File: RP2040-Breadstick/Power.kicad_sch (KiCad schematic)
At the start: 11 parts, among them IC501 LM66200DRLR, U501 MIC5528-3.3YMT-TR

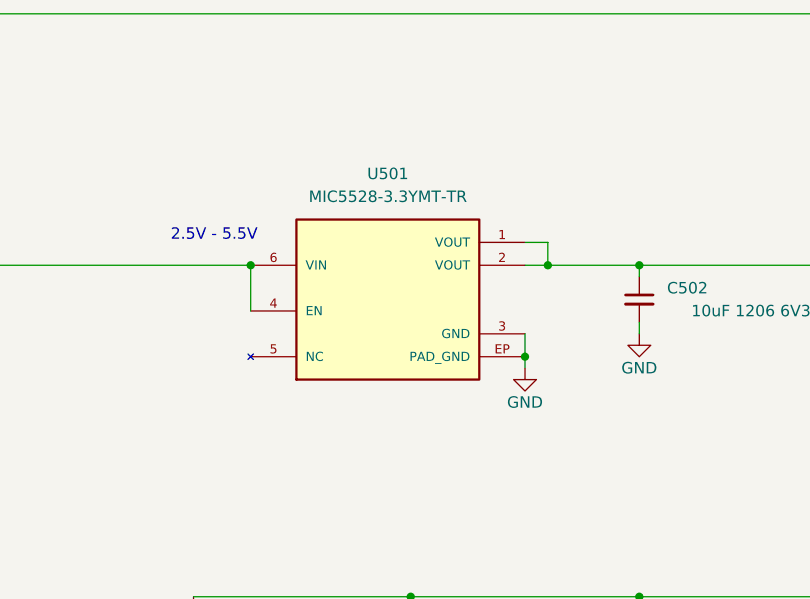
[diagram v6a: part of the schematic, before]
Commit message: Finished assigning I/O pins, perfect is the enemy of good.
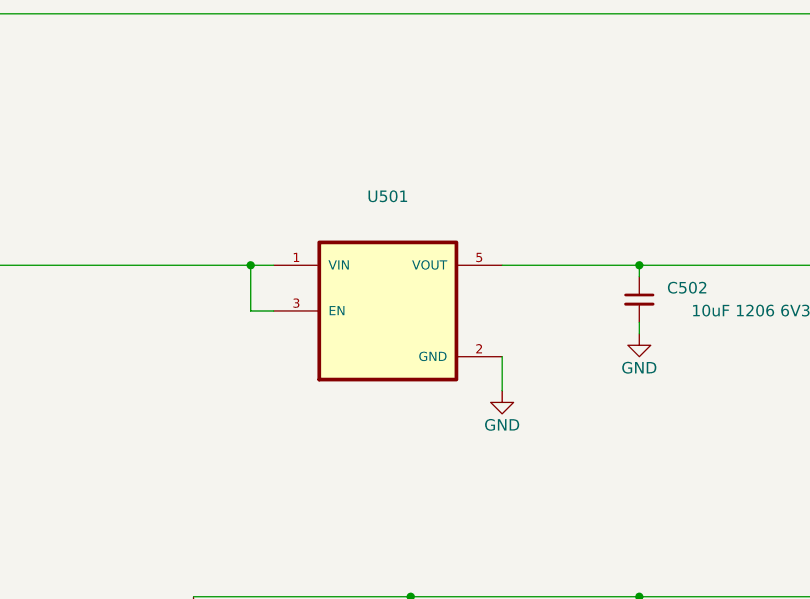
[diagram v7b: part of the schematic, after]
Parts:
- removed U501: MIC5528-3.3YMT-TR, SON40P120X120X60-7N, symbol MIC5528-3.3YMT-TR:MIC5528-3.3YMT-TR
- added U501: (no value), symbol AP2112K-3.3TRG1:AP2112K-3.3TRG1
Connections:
- net 3V3_LDO: now also U501.5 (VOUT)
- net GND: now also U501.2 (GND)
- net VHI: now also U501.1 (VIN), U501.3 (EN)
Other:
- note removed: "2.5V - 5.5V"

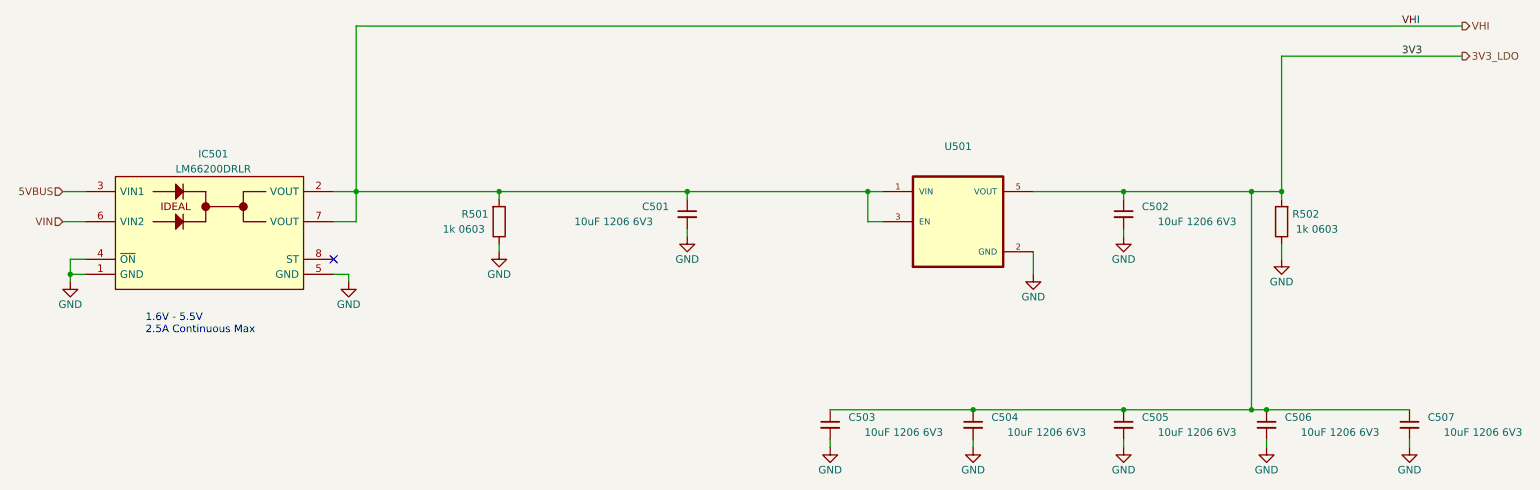
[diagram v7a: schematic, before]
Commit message: replaced switches, upsized some passives to 0603
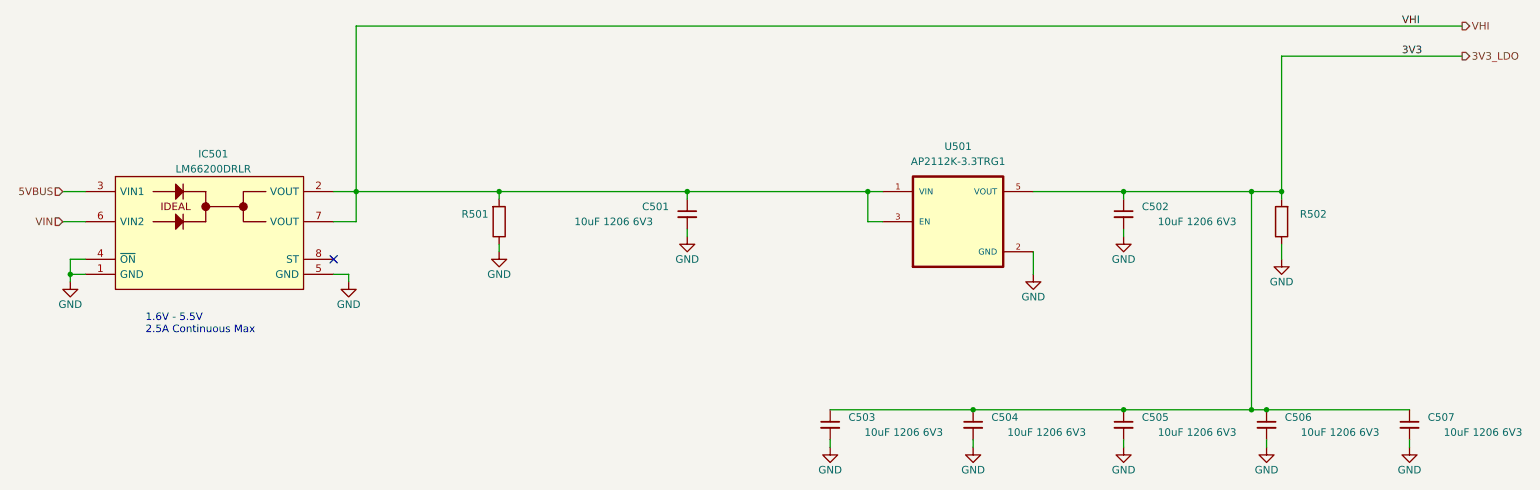
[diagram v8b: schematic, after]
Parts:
- R501: value 1k 0603 -> (none); footprint Resistor_SMD:R_0603_1608Metric -> (none)
- R502: value 1k 0603 -> (none)
- U501: value (none) -> AP2112K-3.3TRG1; footprint (none) -> AP2112K-3:SOT95P285X140-5N
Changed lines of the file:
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@@
   (symbol (lib_id "Device:R") (at 233.68 81.28 180) (unit 1)
     (in_bom yes) (on_board yes)
-    (property "Reference" "R502" (id 0) (at 240.03 80.01 0)
-      (effects (font (size 1.27 1.27)) (justify left))
-    )
-    (property "Value" "1k 0603" (id 1) (at 243.205 82.55 0)
+    (property "Reference" "R502" (id 0) (at 241.3 80.01 0)
+      (effects (font (size 1.27 1.27)) (justify left))
+    )
+    (property "Value" "" (id 1) (at 245.11 82.55 0)
       (effects (font (size 1.27 1.27)) (justify left))
     )
@@
     (in_bom yes) (on_board yes) (fields_autoplaced)
     (property "Reference" "U501" (id 0) (at 179.07 68.58 0))
-    (property "Value" "" (id 1) (at 179.07 71.12 0))
-    (property "Footprint" "" (id 2) (at 179.07 81.28 0)
+    (property "Value" "AP2112K-3.3TRG1" (id 1) (at 179.07 71.12 0))
+    (property "Footprint" "AP2112K-3:SOT95P285X140-5N" (id 2) (at 179.07 81.28 0)
       (effects (font (size 1.27 1.27)) (justify bottom) hide)
     )
@@
       (effects (font (size 1.27 1.27)) (justify left))
     )
-    (property "Value" "1k 0603" (id 1) (at 92.075 82.55 0)
-      (effects (font (size 1.27 1.27)) (justify left))
-    )
-    (property "Footprint" "Resistor_SMD:R_0603_1608Metric" (id 2) (at 99.822 81.28 90)
-      (effects (font (size 1.27 1.27)) hide)
-    )
+    (property "Value" "" (id 1) (at 90.17 82.55 0)
+      (effects (font (size 1.27 1.27)) (justify left))
+    )
+    (property "Footprint" "" (id 2) (at 99.822 81.28 90)
+      (effects (font (size 1.27 1.27)) hide)
+    )
